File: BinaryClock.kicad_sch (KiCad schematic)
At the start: 8 parts, among them U1 4060, U2 4060, U3 4024, U4 4024, U5 4024, U6 4082, U7 4082, U8 4071

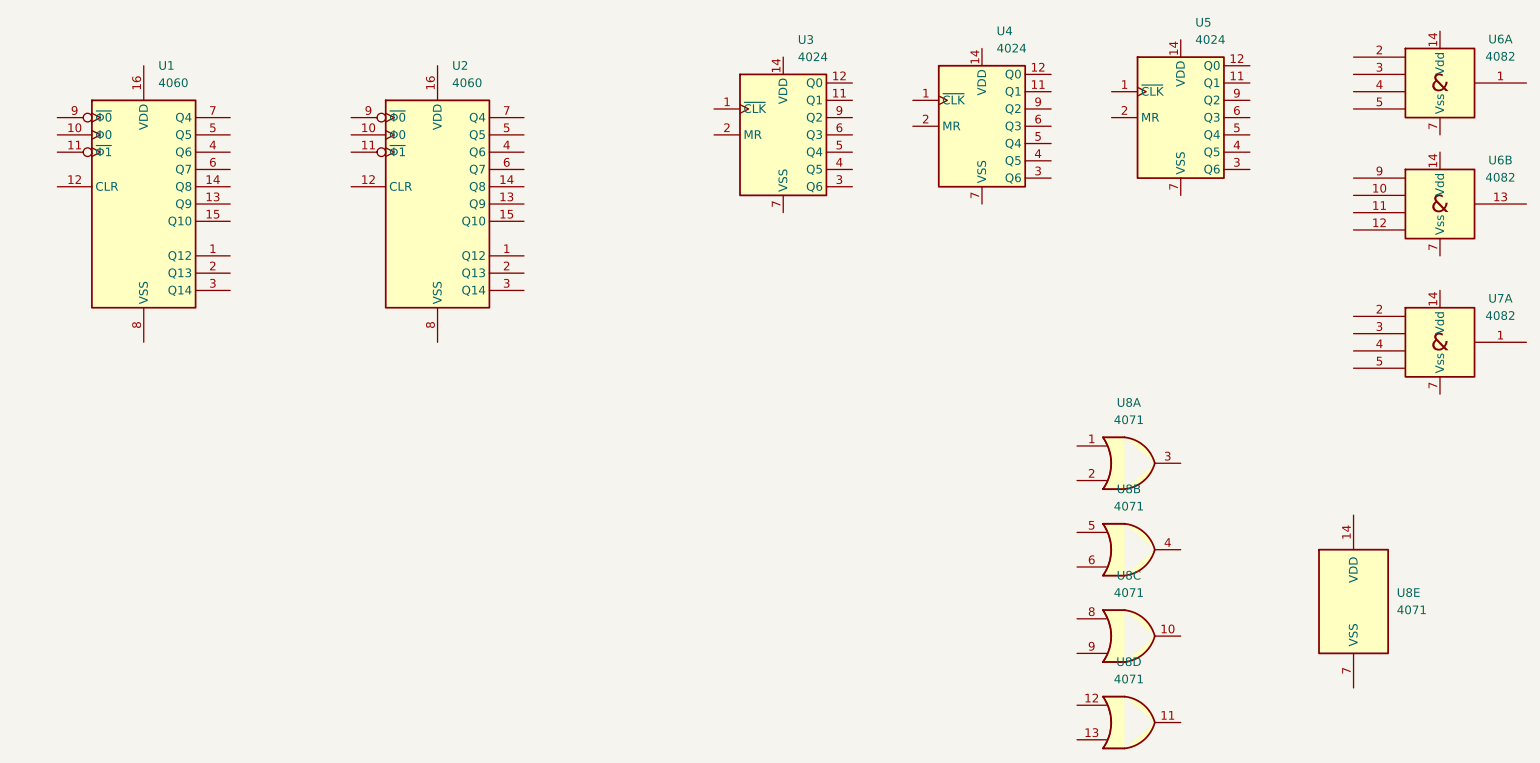
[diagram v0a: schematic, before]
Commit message: making the CLK circuit
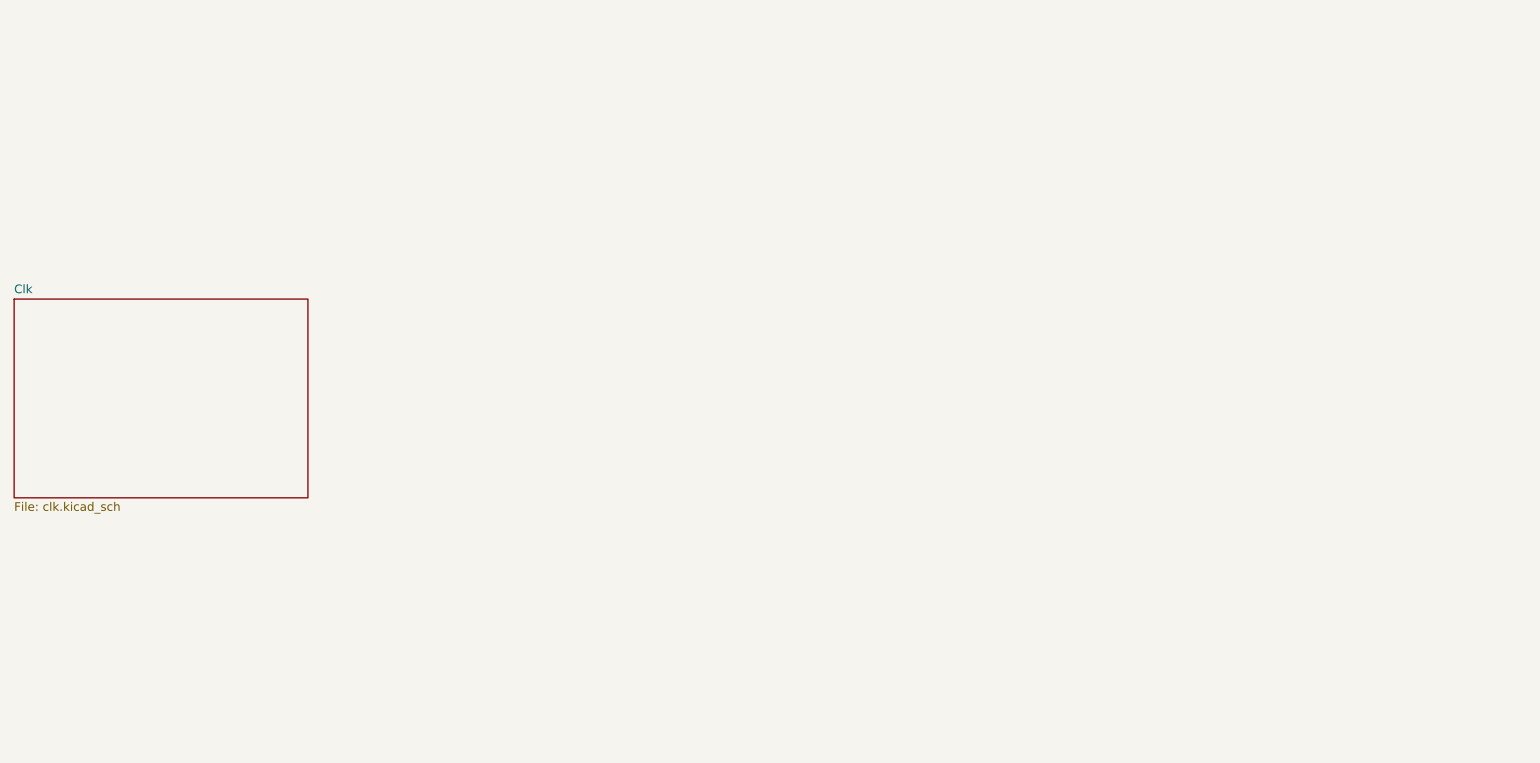
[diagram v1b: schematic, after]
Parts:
- removed U1, U2: 4060, symbol 4xxx:4060
- removed U3, U4, U5: 4024, symbol 4xxx_IEEE:4024
- removed U6, U7: 4082, symbol 4xxx_IEEE:4082
- removed U8: 4071, symbol 4xxx:4071
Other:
- added sheet Clk (clk.kicad_sch)

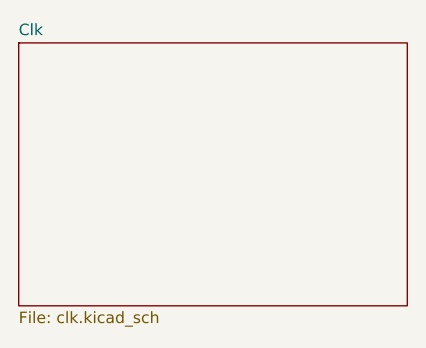
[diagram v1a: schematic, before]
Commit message: CLK circuit finishing the clk circuit
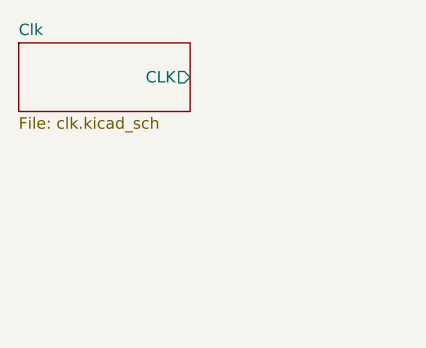
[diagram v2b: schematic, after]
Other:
- sheet Clk ports: added CLK; removed none
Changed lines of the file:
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@@
 	(sheet
 		(at 50.8 90.17)
-		(size 43.18 29.21)
+		(size 19.05 7.62)
 		(exclude_from_sim no)
 		(in_bom yes)
@@
 		)
 		(property "Sheetfile" "clk.kicad_sch"
-			(at 50.8 119.9646 0)
+			(at 50.8 98.3746 0)
 			(show_name no)
 			(do_not_autoplace no)
@@
 			)
 		)
+		(pin "CLK" output
+			(at 69.85 93.98 0)
+			(effects
+				(font
+					(size 1.27 1.27)
+				)
+				(justify right)
+			)
+		)

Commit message: adding the file
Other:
- added sheet Counters (untitled.kicad_sch)
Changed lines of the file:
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@@
+		)
+	)
+	(sheet
+		(at 88.9 88.9)
+		(size 25.4 10.16)
+		(exclude_from_sim no)
+		(in_bom yes)
+		(on_board yes)
+		(dnp no)
+		(fields_autoplaced yes)
+		(stroke
+			(width 0.1524)
+			(type solid)
+		)
+		(fill
+			(color 0 0 0 0)
+		)
+		(property "Sheetname" "Counters"
+			(at 88.9 88.1884 0)
+			(show_name no)
+			(do_not_autoplace no)
+			(effects
+				(font
+					(size 1.27 1.27)
+				)
+				(justify left bottom)
+			)
+		)
+		(property "Sheetfile" "untitled.kicad_sch"
+			(at 88.9 99.6446 0)
+			(show_name no)
+			(do_not_autoplace no)
+			(effects
+				(font
+					(size 1.27 1.27)
+				)
+				(justify left top)
+			)
+		)
+		(instances
+			(project "BinaryClock"
+				(path "/b8db7867-2c41-4996-89b7-85623a375f4b"
+					(page "3")
+				)
+			)
 		)
 	)

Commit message: finishing the min circuit nad conect it to its place
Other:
- sheet Counters ports: added CLK; removed none
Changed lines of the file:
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@@
 	(generator_version "10.0")
 	(paper "A4")
+	(wire
+		(pts
+			(xy 69.85 93.98) (xy 88.9 93.98)
+		)
+		(stroke
+			(width 0)
+			(type default)
+		)
+	)
 	(sheet
 		(at 50.8 90.17)
@@
 			)
 		)
+		(pin "CLK" input
+			(at 88.9 93.98 180)
+			(effects
+				(font
+					(size 1.27 1.27)
+				)
+				(justify left)
+			)
+		)

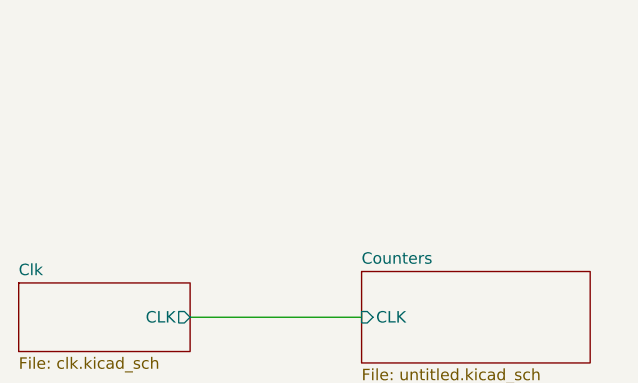
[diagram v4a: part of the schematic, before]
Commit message: Creating the power sheet
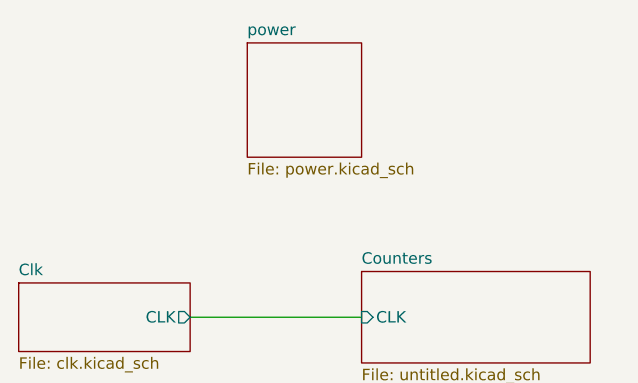
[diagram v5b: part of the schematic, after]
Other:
- added sheet power (power.kicad_sch)
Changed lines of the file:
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@@
+		)
+	)
+	(sheet
+		(at 76.2 63.5)
+		(size 12.7 12.7)
+		(exclude_from_sim no)
+		(in_bom yes)
+		(on_board yes)
+		(dnp no)
+		(fields_autoplaced yes)
+		(stroke
+			(width 0.1524)
+			(type solid)
+		)
+		(fill
+			(color 0 0 0 0)
+		)
+		(property "Sheetname" "power"
+			(at 76.2 62.7884 0)
+			(show_name no)
+			(do_not_autoplace no)
+			(effects
+				(font
+					(size 1.27 1.27)
+				)
+				(justify left bottom)
+			)
+		)
+		(property "Sheetfile" "power.kicad_sch"
+			(at 76.2 76.7846 0)
+			(show_name no)
+			(do_not_autoplace no)
+			(effects
+				(font
+					(size 1.27 1.27)
+				)
+				(justify left top)
+			)
+		)
+		(instances
+			(project "BinaryClock"
+				(path "/b8db7867-2c41-4996-89b7-85623a375f4b"
+					(page "7")
+				)
+			)
 		)
 	)

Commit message: Designing the base circuit of the usb-c
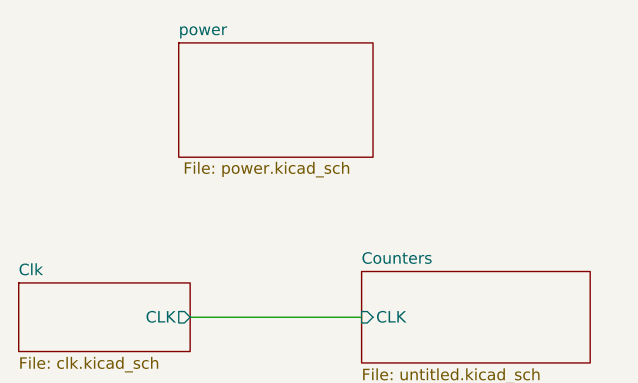
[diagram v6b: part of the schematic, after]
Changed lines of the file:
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@@
 	)
 	(sheet
-		(at 76.2 63.5)
-		(size 12.7 12.7)
+		(at 68.58 63.5)
+		(size 21.59 12.7)
 		(exclude_from_sim no)
 		(in_bom yes)
 		(on_board yes)
 		(dnp no)
-		(fields_autoplaced yes)
 		(stroke
 			(width 0.1524)
@@
 		)
 		(property "Sheetname" "power"
-			(at 76.2 62.7884 0)
+			(at 68.58 62.7884 0)
 			(show_name no)
 			(do_not_autoplace no)
@@
 		)
 		(property "Sheetfile" "power.kicad_sch"
-			(at 76.2 76.7846 0)
+			(at 69.088 76.708 0)
 			(show_name no)
 			(do_not_autoplace no)
